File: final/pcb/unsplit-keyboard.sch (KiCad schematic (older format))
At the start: 16 parts, among them J1 USB_C_Receptacle_USB2.0, SW1 SW_PUSH, U1 ATMEGA32U4, X1 XTAL_GND

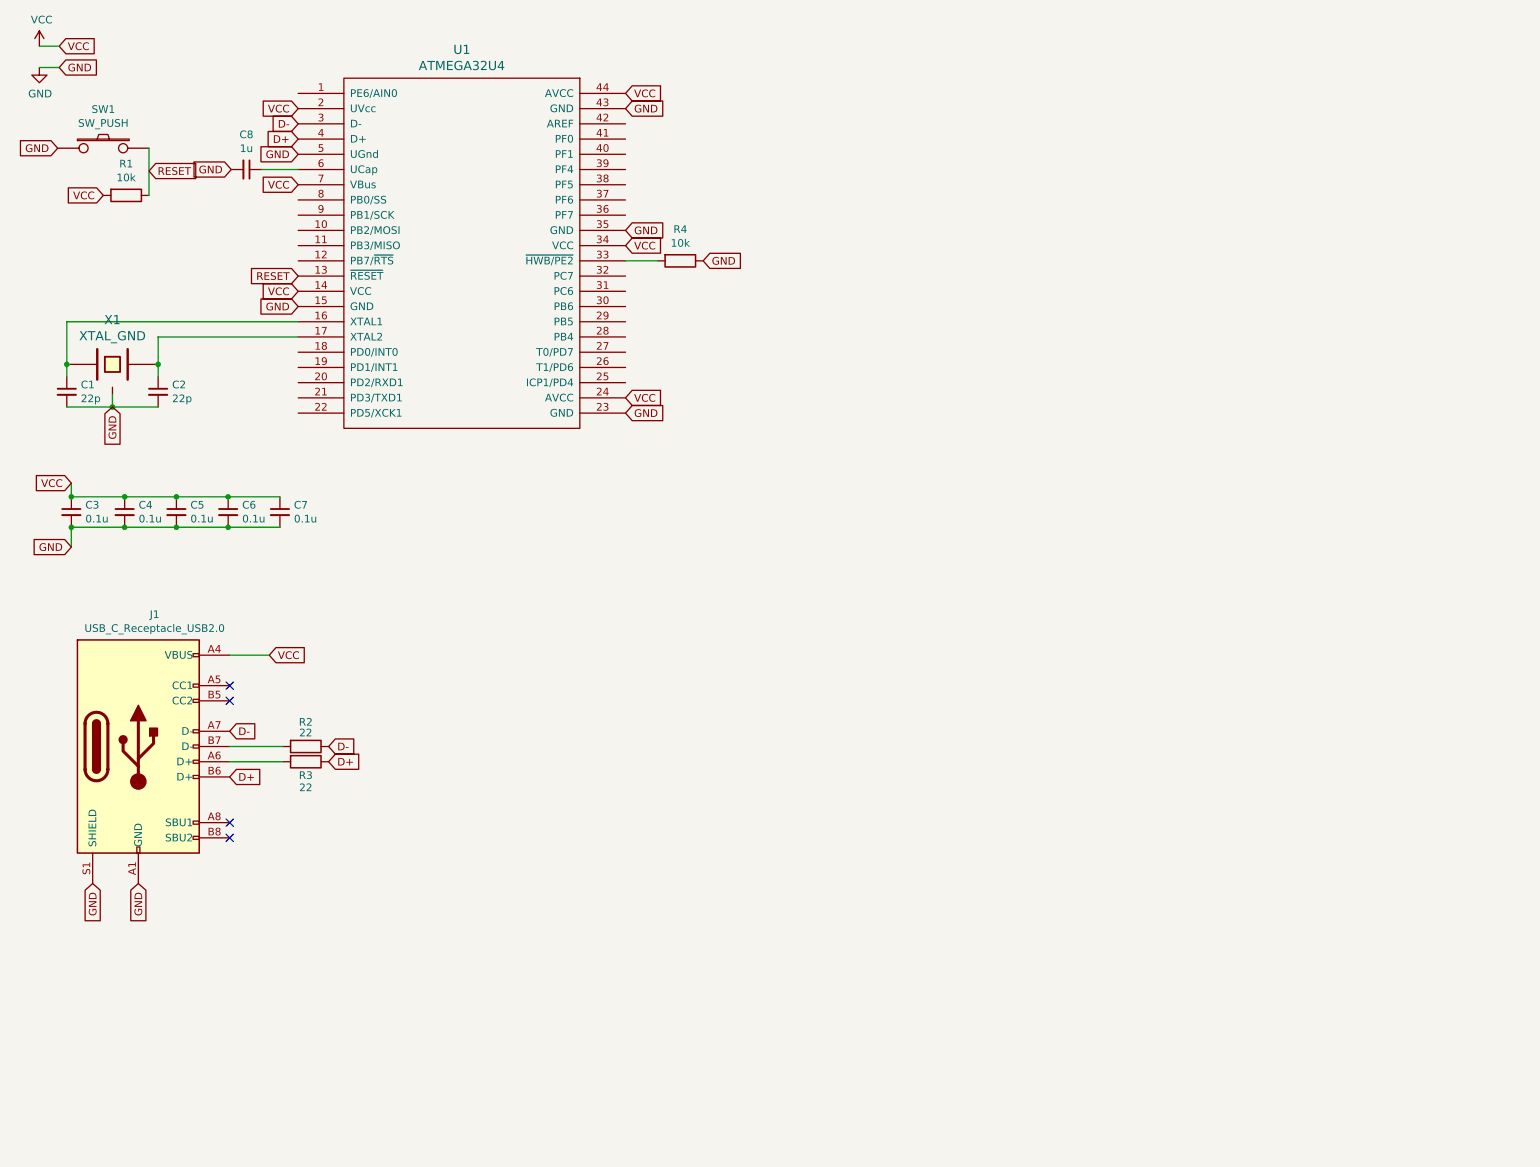
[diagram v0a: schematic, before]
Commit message: fixed almost everything on the entire keyboard
only need to buy new oled panel and test it, then layout new pcb, print them, layout new plate file, print it, and make a new case
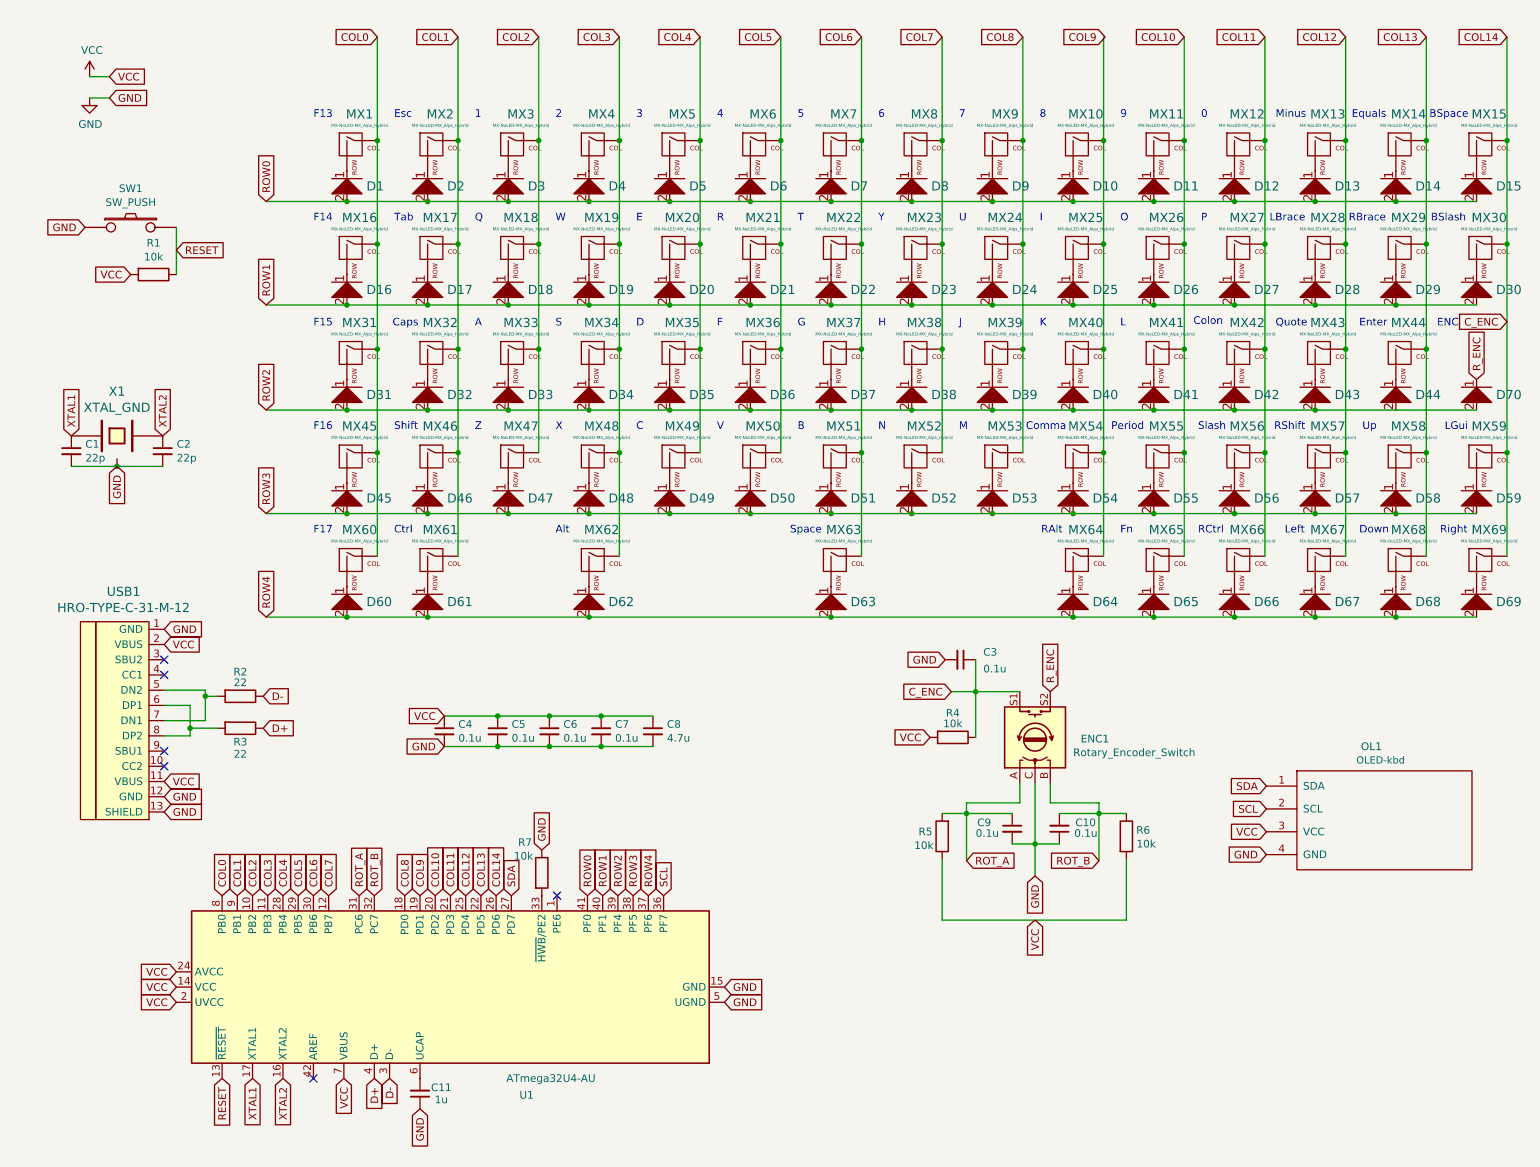
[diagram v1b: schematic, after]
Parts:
- removed J1: USB_C_Receptacle_USB2.0, symbol Connector:USB_C_Receptacle_USB2.0
- removed U1: ATMEGA32U4, symbol KeyboardMasterList:ATMEGA32U4
- added C10, C3, C9: 0.1u, Capacitor_SMD:C_0805_2012Metric, symbol Device:C_Small
- added D1, D10, D11, D12, D13, D14, D15, D16, D17, D18, D19, D2, D20, D21, D22, D23, D24, D25, D26, D27, D28, D29, D3, D30, D31, D32, D33, D34, D35, D36, D37, D38, D39, D4, D40, D41, D42, D43, D44, D45, D46, D47, D48, D49, D5, D50, D51, D52, D53, D54, D55, D56, D57, D58, D59, D6, D60, D61, D62, D63, D64, D65, D66, D67, D68, D69, D7, D70, D8, D9: D, Diode_SMD:D_0805_2012Metric, symbol KeyboardMasterList:D
- added ENC1: Rotary_Encoder_Switch, Rotary_Encoder:RotaryEncoder_Alps_EC11E-Switch_Vertical_H20mm, symbol Device:Rotary_Encoder_Switch
- added MX1, MX10, MX11, MX12, MX13, MX14, MX16, MX18, MX19, MX2, MX20, MX21, MX22, MX23, MX24, MX25, MX26, MX27, MX28, MX29, MX3, MX31, MX33, MX34, MX35, MX36, MX37, MX38, MX39, MX4, MX40, MX41, MX42, MX43, MX45, MX47, MX48, MX49, MX5, MX50, MX51, MX52, MX53, MX54, MX55, MX56, MX58, MX59, MX6, MX60, MX64, MX65, MX66, MX67, MX68, MX69, MX7, MX8, MX9: MX-NoLED-MX_Alps_Hybrid, Keyboard Master List:MX-1U, symbol KeyboardMasterList:MX-NoLED-MX_Alps_Hybrid
- added MX15: MX-NoLED-MX_Alps_Hybrid, Keyboard Master List:MX-2U, symbol KeyboardMasterList:MX-NoLED-MX_Alps_Hybrid
- added MX17, MX30: MX-NoLED-MX_Alps_Hybrid, Keyboard Master List:MX-1.5U, symbol KeyboardMasterList:MX-NoLED-MX_Alps_Hybrid
- added MX32, MX57: MX-NoLED-MX_Alps_Hybrid, Keyboard Master List:MX-1.75U, symbol KeyboardMasterList:MX-NoLED-MX_Alps_Hybrid
- added MX44, MX46: MX-NoLED-MX_Alps_Hybrid, Keyboard Master List:MX-2.25U, symbol KeyboardMasterList:MX-NoLED-MX_Alps_Hybrid
- added MX61, MX62: MX-NoLED-MX_Alps_Hybrid, Keyboard Master List:MX-1.25U, symbol KeyboardMasterList:MX-NoLED-MX_Alps_Hybrid
- added MX63: MX-NoLED-MX_Alps_Hybrid, Keyboard Master List:MX-6.25U, symbol KeyboardMasterList:MX-NoLED-MX_Alps_Hybrid
- added OL1: OLED-kbd, Keyboard Master List:OLED, symbol KeyboardMasterList:OLED-kbd
- added R4, R5, R6: 10k, Resistor_SMD:R_0805_2012Metric, symbol Device:R
- added U1: ATmega32U4-AU, Keebio Parts:ATMEGA32U4-AU, symbol MCU_Microchip_ATmega:ATmega32U4-AU
- added USB1: HRO-TYPE-C-31-M-12, Keebio Parts:USB-C-12-Pin-MidMount, symbol keebio:HRO-TYPE-C-31-M-12
- C1, C2: footprint (none) -> Capacitor_SMD:C_0805_2012Metric
- C11: renamed from C8; footprint (none) -> Capacitor_SMD:C_0805_2012Metric
- C4: renamed from C3; footprint (none) -> Capacitor_SMD:C_0805_2012Metric
- C5: renamed from C4; footprint (none) -> Capacitor_SMD:C_0805_2012Metric
- C6: renamed from C5; footprint (none) -> Capacitor_SMD:C_0805_2012Metric
- C7: renamed from C6; footprint (none) -> Capacitor_SMD:C_0805_2012Metric
- C8: renamed from C7; value 0.1u -> 4.7u; footprint (none) -> Capacitor_SMD:C_0805_2012Metric
- R1, R2, R3: footprint (none) -> Resistor_SMD:R_0805_2012Metric
- R7: renamed from R4; footprint (none) -> Resistor_SMD:R_0805_2012Metric
- SW1: footprint (none) -> Keyboard Master List:SKQG-1155865
- X1: footprint (none) -> Keebio Parts:Crystal_SMD_3225-4pin_3.2x2.5mm
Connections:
- net D+: now also U1.4 (D+)
- net D-: now also U1.3 (D-)
- net GND: now also C11.1, C10.1, C3.2, C9.2, ENC1.C, OL1.4 (GND), U1.15 (GND), U1.23 (GND), U1.35 (GND), U1.43 (GND), U1.5 (UGND), USB1.1 (GND), USB1.12 (GND), USB1.13 (SHIELD); no longer C11.2
- net RESET: now also U1.13 (~RESET)
- net VCC: now also OL1.3 (VCC), R4.2, R5.1, R6.2, U1.14 (VCC), U1.2 (UVCC), U1.24 (AVCC), U1.34 (VCC), U1.44 (AVCC), U1.7 (VBUS), USB1.11 (VBUS), USB1.2 (VBUS)
- net XTAL1: now reaches C1.1, X1.1
- net XTAL1: now also U1.17 (XTAL1)
- net XTAL2: now reaches C2.1, X1.2
- net XTAL2: now also U1.16 (XTAL2)
- net at R7.2: now also U1.33 (~HWB~/PE2)
- net at R3.2: now also USB1.6 (DP1), USB1.8 (DP2)
- net at R2.2: now also USB1.5 (DN2), USB1.7 (DN1)
- new net: C11.2, U1.6 (UCAP)
- new net: D63.1, MX63.2 (ROW)
- new net: D62.1, MX62.2 (ROW)
- new net: D61.1, MX61.2 (ROW)
- new net: D60.1, MX60.2 (ROW)
- new net: D68.1, MX68.2 (ROW)
- new net: D66.1, MX66.2 (ROW)
- new net: D69.1, MX69.2 (ROW)
- new net: D65.1, MX65.2 (ROW)
- new net: D64.1, MX64.2 (ROW)
- new net: MX10.1 (COL), MX25.1 (COL), MX40.1 (COL), MX54.1 (COL), MX64.1 (COL)
- new net: D53.1, MX53.2 (ROW)
- new net: D52.1, MX52.2 (ROW)
- new net: D54.1, MX54.2 (ROW)
- new net: D51.1, MX51.2 (ROW)
- new net: D50.1, MX50.2 (ROW)
- new net: D48.1, MX48.2 (ROW)
- new net: D47.1, MX47.2 (ROW)
- new net: D49.1, MX49.2 (ROW)
- new net: D46.1, MX46.2 (ROW)
- new net: D45.1, MX45.2 (ROW)
- new net: D57.1, MX57.2 (ROW)
- new net: D56.1, MX56.2 (ROW)
- new net: D55.1, MX55.2 (ROW)
- new net: D59.1, MX59.2 (ROW)
- new net: D58.1, MX58.2 (ROW)
- new net: D39.1, MX39.2 (ROW)
- new net: D38.1, MX38.2 (ROW)
- new net: D40.1, MX40.2 (ROW)
- new net: D37.1, MX37.2 (ROW)
- new net: D36.1, MX36.2 (ROW)
- new net: D34.1, MX34.2 (ROW)
- new net: D33.1, MX33.2 (ROW)
- new net: D35.1, MX35.2 (ROW)
- new net: D32.1, MX32.2 (ROW)
- new net: D31.1, MX31.2 (ROW)
- new net: D43.1, MX43.2 (ROW)
- new net: D42.1, MX42.2 (ROW)
- new net: D41.1, MX41.2 (ROW)
- new net: D44.1, MX44.2 (ROW)
- new net: D24.1, MX24.2 (ROW)
- new net: D23.1, MX23.2 (ROW)
- new net: D25.1, MX25.2 (ROW)
- new net: D22.1, MX22.2 (ROW)
- new net: D21.1, MX21.2 (ROW)
- new net: D19.1, MX19.2 (ROW)
- new net: D18.1, MX18.2 (ROW)
- new net: D20.1, MX20.2 (ROW)
- new net: D17.1, MX17.2 (ROW)
- new net: D16.1, MX16.2 (ROW)
- new net: D28.1, MX28.2 (ROW)
- new net: D27.1, MX27.2 (ROW)
- new net: D26.1, MX26.2 (ROW)
- new net: D30.1, MX30.2 (ROW)
- new net: D29.1, MX29.2 (ROW)
- new net: D9.1, MX9.2 (ROW)
- new net: D8.1, MX8.2 (ROW)
- new net: D10.1, MX10.2 (ROW)
- new net: D7.1, MX7.2 (ROW)
- new net: D6.1, MX6.2 (ROW)
- new net: D4.1, MX4.2 (ROW)
- new net: D3.1, MX3.2 (ROW)
- new net: D5.1, MX5.2 (ROW)
- new net: D2.1, MX2.2 (ROW)
- new net: D1.1, MX1.2 (ROW)
- new net: D13.1, MX13.2 (ROW)
- new net: D12.1, MX12.2 (ROW)
- new net: D11.1, MX11.2 (ROW)
- new net: D15.1, MX15.2 (ROW)
- new net: D14.1, MX14.2 (ROW)
- new net: D67.1, MX67.2 (ROW)
- new net COL0: MX1.1 (COL), MX16.1 (COL), MX31.1 (COL), MX45.1 (COL), MX60.1 (COL), U1.8 (PB0)
- new net COL1: MX17.1 (COL), MX2.1 (COL), MX32.1 (COL), MX46.1 (COL), MX61.1 (COL), U1.9 (PB1)
- new net COL10: MX11.1 (COL), MX26.1 (COL), MX41.1 (COL), MX55.1 (COL), MX65.1 (COL), U1.20 (PD2)
- new net COL11: MX12.1 (COL), MX27.1 (COL), MX42.1 (COL), MX56.1 (COL), MX66.1 (COL), U1.21 (PD3)
- new net COL12: MX13.1 (COL), MX28.1 (COL), MX43.1 (COL), MX57.1 (COL), MX67.1 (COL), U1.25 (PD4)
- new net COL13: MX14.1 (COL), MX29.1 (COL), MX44.1 (COL), MX58.1 (COL), MX68.1 (COL), U1.22 (PD5)
- new net COL14: C3.1, ENC1.S1, MX15.1 (COL), MX30.1 (COL), MX59.1 (COL), MX69.1 (COL), R4.1, U1.26 (PD6)
- new net COL2: MX18.1 (COL), MX3.1 (COL), MX33.1 (COL), MX47.1 (COL), U1.10 (PB2)
- new net COL3: MX19.1 (COL), MX34.1 (COL), MX4.1 (COL), MX48.1 (COL), MX62.1 (COL), U1.11 (PB3)
- new net COL4: MX20.1 (COL), MX35.1 (COL), MX49.1 (COL), MX5.1 (COL), U1.28 (PB4)
- new net COL5: MX21.1 (COL), MX36.1 (COL), MX50.1 (COL), MX6.1 (COL), U1.29 (PB5)
- new net COL6: MX22.1 (COL), MX37.1 (COL), MX51.1 (COL), MX63.1 (COL), MX7.1 (COL), U1.30 (PB6)
- new net COL7: MX23.1 (COL), MX38.1 (COL), MX52.1 (COL), MX8.1 (COL), U1.12 (PB7)
- new net COL8: MX24.1 (COL), MX39.1 (COL), MX53.1 (COL), MX9.1 (COL), U1.18 (PD0)
- new net COL9: U1.19 (PD1)
- new net ROT_A: C9.1, ENC1.A, R5.2, U1.31 (PC6)
- new net ROT_B: C10.2, ENC1.B, R6.1, U1.32 (PC7)
- new net ROW0: D1.2, D10.2, D11.2, D12.2, D13.2, D14.2, D15.2, D2.2, D3.2, D4.2, D5.2, D6.2, D7.2, D8.2, D9.2, U1.41 (PF0)
- new net ROW1: D16.2, D17.2, D18.2, D19.2, D20.2, D21.2, D22.2, D23.2, D24.2, D25.2, D26.2, D27.2, D28.2, D29.2, D30.2, U1.40 (PF1)
- new net ROW2: D31.2, D32.2, D33.2, D34.2, D35.2, D36.2, D37.2, D38.2, D39.2, D40.2, D41.2, D42.2, D43.2, D44.2, D70.2, U1.39 (PF4)
- new net ROW3: D45.2, D46.2, D47.2, D48.2, D49.2, D50.2, D51.2, D52.2, D53.2, D54.2, D55.2, D56.2, D57.2, D58.2, D59.2, U1.38 (PF5)
- new net ROW4: D60.2, D61.2, D62.2, D63.2, D64.2, D65.2, D66.2, D67.2, D68.2, D69.2, U1.37 (PF6)
- new net R_ENC: D70.1, ENC1.S2
- new net SCL: OL1.2 (SCL), U1.36 (PF7)
- new net SDA: OL1.1 (SDA), U1.27 (PD7)
- no-connect marks 4 -> 6
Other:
- note added: "0"
- note added: "1"
- note added: "2"
- note added: "3"
- note added: "4"
- note added: "5"
- note added: "6"
- note added: "7"
- note added: "8"
- note added: "9"
- note added: "A"
- note added: "Alt"
- note added: "B"
- note added: "BSlash"
- note added: "BSpace"
- note added: "C"
- note added: "Caps"
- note added: "Colon"
- note added: "Comma"
- note added: "Ctrl"
- note added: "D"
- note added: "Down"
- note added: "E"
- note added: "ENC"
- note added: "Enter"
- note added: "Equals"
- note added: "Esc"
- note added: "F"
- note added: "F13"
- note added: "F14"
- note added: "F15"
- note added: "F16"
- note added: "F17"
- note added: "Fn"
- note added: "G"
- note added: "H"
- note added: "I"
- note added: "J"
- note added: "K"
- note added: "L"
- note added: "LBrace"
- note added: "LGui"
- note added: "Left"
- note added: "M"
- note added: "Minus"
- note added: "N"
- note added: "O"
- note added: "P"
- note added: "Period"
- note added: "Q"
- note added: "Quote"
- note added: "R"
- note added: "RAlt"
- note added: "RBrace"
- note added: "RCtrl"
- note added: "RShift"
- note added: "Right"
- note added: "S"
- note added: "Shift"
- note added: "Slash"
- note added: "Space"
- note added: "T"
- note added: "Tab"
- note added: "U"
- note added: "Up"
- note added: "V"
- note added: "W"
- note added: "X"
- note added: "Y"
- note added: "Z"
- moved on the sheet: C1, C11, C2, C4, C5, C6, C7, C8, R1, R2, R3, R7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

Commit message: firmware files uploaded
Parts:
- added R8, R9: 4.7k, Resistor_SMD:R_0805_2012Metric, symbol Device:R
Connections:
- net SCL: now also R8.1
- net SDA: now also R9.1
- net VCC: now also R8.2, R9.2
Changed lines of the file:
@@
 Text GLabel 3310 5170 0    50   Input ~ 0
 VCC
-$Comp
-L KeyboardMasterList:OLED-kbd OL1
-U 1 1 60EDA0A7
-P 9460 5880
-F 0 "OL1" H 9330 6390 51  0000 L CNN
-F 1 "OLED-kbd" H 9300 6300 47  0000 L CNN
-F 2 "Keyboard Master List:OLED" H 9460 5980 60  0001 C CNN
-F 3 "" H 9460 5980 60  0001 C CNN
-	1    9460 5880
-	1    0    0    -1
-$EndComp
 Text GLabel 8710 5930 0    50   Input ~ 0
 VCC
@@
 Wire Wire Line
 	1160 3530 1460 3530
-Text GLabel 8710 5780 0    50   Input ~ 0
+Text GLabel 8490 5530 0    50   Input ~ 0
 SCL
-Text GLabel 8710 5630 0    50   Input ~ 0
-SDA
 $Comp
 L Device:R R2
@@
 NoConn ~ 2450 7550
 NoConn ~ 4050 6350
+Text GLabel 9010 5440 2    50   Input ~ 0
+VCC
+Text GLabel 9010 5170 2    50   Input ~ 0
+VCC
+Text GLabel 8710 5530 0    50   Input ~ 0
+SDA
+$Comp
+L Device:R R9
+U 1 1 620F1605
+P 8860 5440
+F 0 "R9" V 9010 5450 50  0000 C CNN
+F 1 "4.7k" V 8940 5450 50  0000 C CNN
+F 2 "Resistor_SMD:R_0805_2012Metric" V 8790 5440 50  0001 C CNN
+F 3 "~" H 8860 5440 50  0001 C CNN
+	1    8860 5440
+	0    -1   -1   0
+$EndComp
+Wire Wire Line
+	8490 5170 8710 5170
+Wire Wire Line
+	8490 5780 8710 5780
+$Comp
+L Device:R R8
+U 1 1 62139DB6
+P 8860 5170
+F 0 "R8" V 9010 5180 50  0000 C CNN
+F 1 "4.7k" V 8940 5180 50  0000 C CNN
+F 2 "Resistor_SMD:R_0805_2012Metric" V 8790 5170 50  0001 C CNN
+F 3 "~" H 8860 5170 50  0001 C CNN
+	1    8860 5170
+	0    -1   -1   0
+$EndComp
+Wire Wire Line
+	8490 5170 8490 5780
+Wire Wire Line
+	8710 5630 8710 5440
+$Comp
+L KeyboardMasterList:OLED-kbd OL1
+U 1 1 60EDA0A7
+P 9460 5880
+F 0 "OL1" H 9330 6390 51  0000 L CNN
+F 1 "OLED-kbd" H 9300 6300 47  0000 L CNN
+F 2 "Keyboard Master List:OLED" H 9460 5980 60  0001 C CNN
+F 3 "" H 9460 5980 60  0001 C CNN
+	1    9460 5880
+	1    0    0    -1
+$EndComp
 $EndSCHEMATC

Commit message: everything but simulation done
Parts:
- removed R8, R9: 4.7k, Resistor_SMD:R_0805_2012Metric, symbol Device:R
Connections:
- net COL10: now also U1.25 (PD4); no longer U1.20 (PD2)
- net COL11: now also U1.22 (PD5); no longer U1.21 (PD3)
- net COL12: now also U1.26 (PD6); no longer U1.25 (PD4)
- net COL13: now also U1.27 (PD7); no longer U1.22 (PD5)
- net COL14: now also U1.36 (PF7); no longer U1.26 (PD6)
- net COL8: now also U1.20 (PD2); no longer U1.18 (PD0)
- net COL9: now also MX10.1 (COL), MX25.1 (COL), MX40.1 (COL), MX54.1 (COL), MX64.1 (COL), U1.21 (PD3); no longer U1.19 (PD1)
- net SCL: now also U1.18 (PD0); no longer U1.36 (PF7)
- net SDA: now also U1.19 (PD1); no longer U1.27 (PD7)
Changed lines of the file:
@@
 Wire Wire Line
 	1160 3530 1460 3530
-Text GLabel 8490 5530 0    50   Input ~ 0
+Text GLabel 8710 5780 0    50   Input ~ 0
 SCL
 $Comp
@@
 Text GLabel 4550 6350 1    50   Input ~ 0
 ROW3
+Text GLabel 4750 6350 1    50   Input ~ 0
+COL14
+Text GLabel 3750 6350 1    50   Input ~ 0
+COL13
 Text GLabel 3650 6350 1    50   Input ~ 0
-COL14
-Text GLabel 3550 6350 1    50   Input ~ 0
-COL13
-Text GLabel 3450 6350 1    50   Input ~ 0
 COL12
 Text GLabel 2550 6350 1    50   Input ~ 0
 COL7
+Text GLabel 3550 6350 1    50   Input ~ 0
+COL11
+Text GLabel 3450 6350 1    50   Input ~ 0
+COL10
 Text GLabel 3350 6350 1    50   Input ~ 0
-COL11
+COL9
 Text GLabel 3250 6350 1    50   Input ~ 0
-COL10
-Text GLabel 3150 6350 1    50   Input ~ 0
-COL9
-Text GLabel 3050 6350 1    50   Input ~ 0
 COL8
 Text GLabel 4650 6350 1    50   Input ~ 0
 ROW4
-Text GLabel 3750 6350 1    50   Input ~ 0
+Text GLabel 3150 6350 1    50   Input ~ 0
 SDA
-Text GLabel 4750 6350 1    50   Input ~ 0
+Text GLabel 3050 6350 1    50   Input ~ 0
 SCL
 Text GLabel 6740 6120 2    50   Input ~ 0
@@
 Text GLabel 7110 710  0    50   Input ~ 0
 COL8
-Text GLabel 7650 710  0    50   Input ~ 0
+Text GLabel 7640 710  0    50   Input ~ 0
 COL9
 Text GLabel 8170 710  0    50   Input ~ 0
@@
 Text GLabel 10090 2960 1    50   Input ~ 0
 R_ENC
-Wire Wire Line
-	10290 2070 10290 3440
 Text GLabel 6640 5010 0    50   Input ~ 0
 C_ENC
@@
 R_ENC
 NoConn ~ 2450 7550
-NoConn ~ 4050 6350
-Text GLabel 9010 5440 2    50   Input ~ 0
-VCC
-Text GLabel 9010 5170 2    50   Input ~ 0
-VCC
-Text GLabel 8710 5530 0    50   Input ~ 0
+Text GLabel 8710 5630 0    50   Input ~ 0
 SDA
-$Comp
-L Device:R R9
-U 1 1 620F1605
-P 8860 5440
-F 0 "R9" V 9010 5450 50  0000 C CNN
-F 1 "4.7k" V 8940 5450 50  0000 C CNN
-F 2 "Resistor_SMD:R_0805_2012Metric" V 8790 5440 50  0001 C CNN
-F 3 "~" H 8860 5440 50  0001 C CNN
-	1    8860 5440
-	0    -1   -1   0
-$EndComp
-Wire Wire Line
-	8490 5170 8710 5170
-Wire Wire Line
-	8490 5780 8710 5780
-$Comp
-L Device:R R8
-U 1 1 62139DB6
-P 8860 5170
-F 0 "R8" V 9010 5180 50  0000 C CNN
-F 1 "4.7k" V 8940 5180 50  0000 C CNN
-F 2 "Resistor_SMD:R_0805_2012Metric" V 8790 5170 50  0001 C CNN
-F 3 "~" H 8860 5170 50  0001 C CNN
-	1    8860 5170
-	0    -1   -1   0
-$EndComp
-Wire Wire Line
-	8490 5170 8490 5780
-Wire Wire Line
-	8710 5630 8710 5440
 $Comp
 L KeyboardMasterList:OLED-kbd OL1
@@
 	1    0    0    -1
 $EndComp
+Wire Wire Line
+	10290 2070 10290 3440
+NoConn ~ 4050 6350
 $EndSCHEMATC
